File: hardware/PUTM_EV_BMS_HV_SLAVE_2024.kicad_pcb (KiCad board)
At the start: 2 copper layers, 187 parts, among them IC1 LTC6804HG-1#PBF, IC2 LTC6804HG-1#PBF, J1 L_LTC_CONN, J2 R_LTC_CONN, Q1 BCP56, Q10 CPH3351, Q11 CPH3351, Q12 BCP56, Q13 CPH3351, Q14 CPH3351, Q15 CPH3351, Q16 CPH3351, Q17 CPH3351, Q18 CPH3351, Q19 CPH3351, Q2 CPH3351, Q20 CPH3351, Q21 CPH3351, Q22 CPH3351, Q3 CPH3351, Q4 CPH3351, Q5 CPH3351, Q6 CPH3351, Q7 CPH3351, Q8 CPH3351, Q9 CPH3351

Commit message: spaced out version
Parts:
- removed C10, C11, C12, C13, C14, C15, C16, C17, C25, C26, C27, C28, C29, C30, C31, C32, C33, C34, C35, C36, C37, C38, C8, C9: 10nF, Capacitor_SMD:C_0603_1608Metric
- removed R1, R55, R56, R57, R58, R6: 10k, Resistor_SMD:R_0603_1608Metric
- removed R16, R24, R36, R40, R44, R48, R49, R50, R62, R66, R70, R74, R78, R82, R86, R90, R94, R98: 100, Resistor_SMD:R_0603_1608Metric
- added CN1: 100nF, Samacsys:CA064X104K4RACAUTO, F.Cu at (208.0, 95.5)
- added CN2: 100nF, Samacsys:CA064X104K4RACAUTO, F.Cu at (147.1, 52.5)
- added CN3: 100nF, Samacsys:CA064X104K4RACAUTO, F.Cu at (208.0, 91.2)
- added CN4: 100nF, Samacsys:CA064X104K4RACAUTO, F.Cu at (147.1, 56.8)
- added CN5: 100nF, Samacsys:CA064X104K4RACAUTO, F.Cu at (208.0, 86.8)
- added CN6: 100nF, Samacsys:CA064X104K4RACAUTO, F.Cu at (147.1, 61.1)
- added CN7: 100nF, Samacsys:CA064X104K4RACAUTO, F.Cu at (227.4, 88.7)
- added CN8: 100nF, Samacsys:CA064X104K4RACAUTO, F.Cu at (127.6, 59.3)
- added FL1: DLW21SN501SK2L, Samacsys:DLW21SN121HQ2L, F.Cu at (209.0, 80.9)
- added HS1: PAD, Connector_Wire:SolderWirePad_1x01_SMD_1x2mm, B.Cu at (196.7, 82.2)
- added HS10: PAD, Connector_Wire:SolderWirePad_1x01_SMD_1x2mm, B.Cu at (193.2, 95.8)
- added HS11: PAD, Connector_Wire:SolderWirePad_1x01_SMD_1x2mm, B.Cu at (161.8, 52.2)
- added HS12: PAD, Connector_Wire:SolderWirePad_1x01_SMD_1x2mm, B.Cu at (200.3, 65.8)
- added HS13: PAD, Connector_Wire:SolderWirePad_1x01_SMD_1x2mm, B.Cu at (214.3, 65.8)
- added HS14: PAD, Connector_Wire:SolderWirePad_1x01_SMD_1x2mm, B.Cu at (217.8, 52.2)
- added HS15: PAD, Connector_Wire:SolderWirePad_1x01_SMD_1x2mm, B.Cu at (158.3, 65.8)
- added HS16: PAD, Connector_Wire:SolderWirePad_1x01_SMD_1x2mm, B.Cu at (189.8, 52.2)
- added HS17: PAD, Connector_Wire:SolderWirePad_1x01_SMD_1x2mm, B.Cu at (203.8, 52.2)
- added HS18: PAD, Connector_Wire:SolderWirePad_1x01_SMD_1x2mm, B.Cu at (175.8, 52.2)
- added HS19: PAD, Connector_Wire:SolderWirePad_1x01_SMD_1x2mm, B.Cu at (186.3, 65.8)
- added HS2: PAD, Connector_Wire:SolderWirePad_1x01_SMD_1x2mm, B.Cu at (182.7, 82.2)
- added HS20: PAD, Connector_Wire:SolderWirePad_1x01_SMD_1x2mm, B.Cu at (172.3, 65.8)
- added HS3: PAD, Connector_Wire:SolderWirePad_1x01_SMD_1x2mm, B.Cu at (168.7, 82.2)
- added HS4: PAD, Connector_Wire:SolderWirePad_1x01_SMD_1x2mm, B.Cu at (154.7, 82.2)
- added HS5: PAD, Connector_Wire:SolderWirePad_1x01_SMD_1x2mm, B.Cu at (140.7, 82.2)
- added HS6: PAD, Connector_Wire:SolderWirePad_1x01_SMD_1x2mm, B.Cu at (137.2, 95.8)
- added HS7: PAD, Connector_Wire:SolderWirePad_1x01_SMD_1x2mm, B.Cu at (151.2, 95.8)
- added HS8: PAD, Connector_Wire:SolderWirePad_1x01_SMD_1x2mm, B.Cu at (165.2, 95.8)
- added HS9: PAD, Connector_Wire:SolderWirePad_1x01_SMD_1x2mm, B.Cu at (179.2, 95.8)
- added J3: M80-5100442, Samacsys:M80-51004YY, F.Cu at (225.2, 72.6)
- added J4: M80-5100442, Samacsys:M80-51004YY, F.Cu at (129.8, 74.3)
- added JP1: MES, Jumper:SolderJumper-2_P1.3mm_Bridged2Bar_RoundedPad1.0x1.5mm, F.Cu at (205.3, 59.0)
- added RN1: 100, Samacsys:EXBV8V101JV, F.Cu at (204.2, 95.5)
- added RN2: 100, Samacsys:EXBV8V101JV, F.Cu at (150.8, 52.5)
- added RN3: 100, Samacsys:EXBV8V101JV, F.Cu at (204.2, 91.2)
- added RN4: 100, Samacsys:EXBV8V101JV, F.Cu at (150.8, 56.8)
- added RN5: 100, Samacsys:EXBV8V101JV, F.Cu at (204.2, 86.8)
- added RN6: 100, Samacsys:EXBV8V101JV, F.Cu at (150.8, 61.1)
- added RN7: 10k, Samacsys:EXBV8V101JV, F.Cu at (227.4, 85.0)
- added RN8: 10k, Samacsys:EXBV8V101JV, F.Cu at (127.6, 63.1)
- added T1: HM1236NL, Samacsys:HM1236NL, F.Cu at (216.4, 73.6)
- added T3: HM1236NL, Samacsys:HM1236NL, F.Cu at (138.6, 73.3)
- C18, C23, C24, C3, Q1, Q10, Q11, Q12, Q13, Q14, Q15, Q16, Q17, Q18, Q19, Q2, Q20, Q21, Q22, Q3, Q4, Q5, Q6, Q7, Q8, Q9, R13, R17, R21, R25, R29, R33, R37, R41, R45, R5, R53, R59, R63, R67, R71, R75, R79, R83, R87, R9, R91, R95: moved to B.Cu
- C4, C5: value 10nF -> 100nF
- R12, R20, R28, R32: value 100 -> 120
- moved R12 293.6 mm to (220.9, 88.7), turned to -90 degrees
- moved C4 253.4 mm to (224.5, 88.7), turned to -90 degrees
- moved C2 251.5 mm to (222.1, 93.5), turned to -90 degrees
- moved C1 250.2 mm to (220.6, 93.5), turned to -90 degrees
- moved R2 249.3 mm to (224.5, 85.0), turned to 90 degrees
- moved C6 249.1 mm to (220.2, 81.5), turned to 180 degrees
- moved C3 247.1 mm to (218.2, 85.8)
- moved C18 240.9 mm to (215.8, 84.2)
- moved R5 239.0 mm to (214.2, 85.8)
- moved R7 237.1 mm to (216.2, 83.5), turned to 180 degrees
- moved R8 234.1 mm to (213.2, 83.5), turned to 180 degrees
- moved R4 232.3 mm to (207.5, 83.5), turned to 180 degrees
- moved C19 229.4 mm to (204.5, 83.5), turned to 180 degrees
- moved Q1 222.3 mm to (215.1, 91.2), turned to -90 degrees
- moved IC1 215.0 mm to (215.1, 91.2)
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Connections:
- net /L_LTC/DCH1/S renamed /L_LTC/S1
- net /L_LTC/DCH10/CO+ renamed /L_LTC/C11
- net /L_LTC/DCH10/S renamed /L_LTC/S11
- net /L_LTC/DCH2/S renamed /L_LTC/S2
- net /L_LTC/DCH3/S renamed /L_LTC/S3
- net /L_LTC/DCH4/S renamed /L_LTC/S4
- net /L_LTC/DCH5/S renamed /L_LTC/S5
- net /L_LTC/DCH6/S renamed /L_LTC/S7
- net /L_LTC/DCH7/S renamed /L_LTC/S8
- net /L_LTC/DCH8/S renamed /L_LTC/S9
- net /L_LTC/DCH9/S renamed /L_LTC/S10
- net /R_LTC/DCH1/S renamed /R_LTC/S1
- net /R_LTC/DCH10/CO+ renamed /R_LTC/C11
- net /R_LTC/DCH10/S renamed /R_LTC/S11
- net /R_LTC/DCH2/S renamed /R_LTC/S2
- net /R_LTC/DCH3/S renamed /R_LTC/S3
- net /R_LTC/DCH4/S renamed /R_LTC/S4
- net /R_LTC/DCH5/CO+ renamed /R_LTC/C5
- net /R_LTC/DCH5/S renamed /R_LTC/S5
- net /R_LTC/DCH6/S renamed /R_LTC/S7
- net /R_LTC/DCH7/S renamed /R_LTC/S8
- net /R_LTC/DCH8/S renamed /R_LTC/S9
- net /R_LTC/DCH9/S renamed /R_LTC/S10
- C4 pad 1: /TH1+ -> /TH5+
- C5 pad 1: /TH2+ -> /TH10+
- C5 pad 2: /C1- -> /C11-
- C6 pad 1: /TH3+ -> Net-(C6-Pad1)
- C6 pad 2: /C1- -> /C11-
- C7 pad 1: /TH4+ -> /C1-
- C7 pad 2: /C1- -> Net-(C7-Pad2)
- D3 pad 1: /C2+ -> /C2_SW+
- D6 pad 1: /SW_C5+ -> /C5+
- IC1 pad 10: /L_LTC/DCH7/CO+ -> /L_LTC/C8
- IC1 pad 12: /L_LTC/DCH6/CO+ -> /L_LTC/C7
- IC1 pad 14: /L_LTC/DCH5/CO+ -> /L_LTC/C5
- IC1 pad 15: unconnected-(IC1-S6-Pad15) -> /L_LTC/S6
- IC1 pad 16: /L_LTC/DCH5/CO+ -> /L_LTC/C5
- IC1 pad 18: /L_LTC/DCH4/CO+ -> /L_LTC/C4
- IC1 pad 20: /L_LTC/DCH3/CO+ -> /L_LTC/C3
- IC1 pad 22: /L_LTC/DCH2/CO+ -> /L_LTC/C2
- IC1 pad 24: /L_LTC/DCH1/CO+ -> /L_LTC/C1
- IC1 pad 26: /L_LTC/DCH1/F- -> /L_LTC/C0
- IC1 pad 3: unconnected-(IC1-S12-Pad3) -> /L_LTC/S12
- IC1 pad 33: unconnected-(IC1-GPIO5-Pad33) -> /TH5+
- IC1 pad 6: /L_LTC/DCH10/F- -> /L_LTC/C10
- IC1 pad 8: /L_LTC/DCH8/CO+ -> /L_LTC/C9
- IC2 pad 10: /R_LTC/DCH7/CO+ -> /R_LTC/C8
- IC2 pad 12: /R_LTC/DCH6/CO+ -> /R_LTC/C7
- IC2 pad 15: unconnected-(IC2-S6-Pad15) -> /R_LTC/S6
- IC2 pad 18: /R_LTC/DCH4/CO+ -> /R_LTC/C4
- IC2 pad 20: /R_LTC/DCH3/CO+ -> /R_LTC/C3
- IC2 pad 22: /R_LTC/DCH2/CO+ -> /R_LTC/C2
- IC2 pad 24: /R_LTC/DCH1/CO+ -> /R_LTC/C1
- IC2 pad 26: /R_LTC/DCH1/F- -> /R_LTC/C0
- IC2 pad 27: /TH5+ -> /TH6+
- IC2 pad 28: /TH6+ -> /TH7+
- IC2 pad 29: /TH7+ -> /TH8+
- IC2 pad 3: unconnected-(IC2-S12-Pad3) -> /R_LTC/S12
- IC2 pad 32: /TH8+ -> /TH9+
- IC2 pad 33: unconnected-(IC2-GPIO5-Pad33) -> /TH10+
- IC2 pad 41: /L_LTC/IMB -> /R_LTC/IMA
- IC2 pad 42: /L_LTC/IPB -> /R_LTC/IPA
- IC2 pad 6: /R_LTC/DCH10/F- -> /R_LTC/C10
- IC2 pad 8: /R_LTC/DCH8/CO+ -> /R_LTC/C9
- J1 pad 10: /C1- -> /TH5+
- J1 pad 11: /TH3+ -> /C1-
- J1 pad 13: /TH2+ -> /TH3+
- J1 pad 14: /C1- -> /TH4+
- J1 pad 6: /C1- -> unconnected-(J1-Pin_6-Pad6)
- J1 pad 9: /TH4+ -> /TH2+
- J2 pad 10: /C11- -> /TH10+
- J2 pad 11: /TH7+ -> /C11-
- J2 pad 13: /TH6+ -> unconnected-(J2-Pin_13-Pad13)
- J2 pad 14: /C11- -> /TH9+
- J2 pad 15: unconnected-(J2-Pin_15-Pad15) -> /TH8+
- J2 pad 5: /TH5+ -> /TH6+
- J2 pad 6: /C11- -> unconnected-(J2-Pin_6-Pad6)
- J2 pad 9: /TH8+ -> /TH7+
- Q3 pad 2: /C2+ -> /C2_SW+
- Q6 pad 2: /SW_C5+ -> /C5+
- R12 pad 1: /L_LTC/DCH1/CO+ -> /IPA
- R12 pad 2: /C1+ -> /IMA
- R17 pad 2: /C2+ -> /C2_SW+
- R2 pad 1: /L_LTC/VREF2 -> /TH5+
- R2 pad 2: /TH2+ -> /L_LTC/VREF2
- R20 pad 1: /L_LTC/DCH3/CO+ -> /L_LTC/IPB
- R20 pad 2: /C3+ -> /L_LTC/IMB
- R28 pad 1: /L_LTC/DCH5/CO+ -> /R_LTC/IPA
- R28 pad 2: /SW_C5+ -> /R_LTC/IMA
- R29 pad 2: /SW_C5+ -> /C5+
- R3 pad 1: /L_LTC/VREF2 -> /TH10+
- R3 pad 2: /TH3+ -> /R_LTC/VREF2
- R32 pad 1: /L_LTC/DCH6/CO+ -> /IPB
- R32 pad 2: /C6+ -> /IMB
- S1 pad 1: /C5+ -> /C2+
- S1 pad 2: /SW_C5+ -> /C2_SW+
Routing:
- net /R_LTC/C0: track 0.00 -> 14.3 mm
- net /L_LTC/C0: track 0.00 -> 14.3 mm
- net /R_LTC/C5: track 0.00 -> 10.3 mm
- net /L_LTC/C5: track 0.00 -> 10.3 mm
- net /R_LTC/C11: track 0.00 -> 10.2 mm
- net /L_LTC/C11: track 0.00 -> 10.2 mm
- net Net-(Q1-C): track 0.00 -> 10.1 mm
- net Net-(Q12-C): track 0.00 -> 10.1 mm
- net /L_LTC/VREG: track 0.00 -> 8.94 mm, vias 0 -> 1
- net /R_LTC/VREG: track 0.00 -> 8.68 mm, vias 0 -> 1
- net /L_LTC/C9: track 0.00 -> 8.29 mm
- net /R_LTC/C9: track 0.00 -> 8.29 mm
- net /R_LTC/C4: track 0.00 -> 8.02 mm
- net /L_LTC/C4: track 0.00 -> 8.02 mm
- net /L_LTC/VREF2: track 0.00 -> 8.01 mm
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- added copper zone on B.Cu, net Net-(Q10-D)
- added copper zone on B.Cu, net Net-(Q11-D)
- added copper zone on B.Cu, net Net-(Q13-D)
- added copper zone on B.Cu, net Net-(Q14-D)
- added copper zone on B.Cu, net Net-(Q15-D)
- added copper zone on B.Cu, net Net-(Q16-D)
- added copper zone on B.Cu, net Net-(Q17-D)
- added copper zone on B.Cu, net Net-(Q18-D)
- added copper zone on B.Cu, net Net-(Q19-D)
- added copper zone on B.Cu, net Net-(Q2-D)
- added copper zone on B.Cu, net Net-(Q20-D)
- added copper zone on B.Cu, net Net-(Q21-D)
- added copper zone on B.Cu, net Net-(Q22-D)
- added copper zone on B.Cu, net Net-(Q3-D)
- added copper zone on B.Cu, net Net-(Q4-D)
- added copper zone on B.Cu, net Net-(Q5-D)
- added copper zone on B.Cu, net Net-(Q6-D)
- added copper zone on B.Cu, net Net-(Q7-D)
- added copper zone on B.Cu, net Net-(Q8-D)
- added copper zone on B.Cu, net Net-(Q9-D)
- added copper zone on B.Cu, net THERMAL
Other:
- board outline added: 105 x 48 mm
- copper layers 2 -> 4

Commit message: finished layout
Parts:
- removed HS1, HS10, HS11, HS12, HS13, HS14, HS15, HS16, HS17, HS18, HS19, HS2, HS20, HS3, HS4, HS5, HS6, HS7, HS8, HS9: PAD, Connector_Wire:SolderWirePad_1x01_SMD_1x2mm
- added F1: 6V/6A, Samacsys:1206L075SLYR, B.Cu at (193.8, 82.2)
- added F10: 6V/6A, Samacsys:1206L075SLYR, B.Cu at (198.1, 95.8)
- added F11: 6V/6A, Samacsys:1206L075SLYR, B.Cu at (156.9, 52.2)
- added F12: 6V/6A, Samacsys:1206L075SLYR, B.Cu at (203.2, 65.8)
- added F13: 6V/6A, Samacsys:1206L075SLYR, B.Cu at (217.2, 65.8)
- added F14: 6V/6A, Samacsys:1206L075SLYR, B.Cu at (212.9, 52.2)
- added F15: 6V/6A, Samacsys:1206L075SLYR, B.Cu at (161.2, 65.8)
- added F16: 6V/6A, Samacsys:1206L075SLYR, B.Cu at (184.9, 52.2)
- added F17: 6V/6A, Samacsys:1206L075SLYR, B.Cu at (198.9, 52.2)
- added F18: 6V/6A, Samacsys:1206L075SLYR, B.Cu at (170.9, 52.2)
- added F19: 6V/6A, Samacsys:1206L075SLYR, B.Cu at (189.2, 65.8)
- added F2: 6V/6A, Samacsys:1206L075SLYR, B.Cu at (179.8, 82.2)
- added F20: 6V/6A, Samacsys:1206L075SLYR, B.Cu at (175.2, 65.8)
- added F3: 6V/6A, Samacsys:1206L075SLYR, B.Cu at (165.8, 82.2)
- added F4: 6V/6A, Samacsys:1206L075SLYR, B.Cu at (151.8, 82.2)
- added F5: 6V/6A, Samacsys:1206L075SLYR, B.Cu at (137.8, 82.2)
- added F6: 6V/6A, Samacsys:1206L075SLYR, B.Cu at (142.1, 95.8)
- added F7: 6V/6A, Samacsys:1206L075SLYR, B.Cu at (156.1, 95.8)
- added F8: 6V/6A, Samacsys:1206L075SLYR, B.Cu at (170.1, 95.8)
- added F9: 6V/6A, Samacsys:1206L075SLYR, B.Cu at (184.1, 95.8)
- added J5: Conn_01x01_Pin, Connector_Wire:SolderWire-0.1sqmm_1x01_D0.4mm_OD1mm_Relief, F.Cu at (133.8, 76.6)
- added J6: Conn_01x01_Pin, Connector_Wire:SolderWire-0.1sqmm_1x01_D0.4mm_OD1mm_Relief, F.Cu at (221.2, 71.4)
- added REF**: plate, Samacsys:plate, B.Cu at (177.5, 74.0)
- R13, R17, R21, R25, R29, R33, R37, R41, R45, R59, R63, R67, R71, R75, R79, R83, R87, R9, R91, R95: footprint Resistor_SMD:R_2512_6332Metric -> Samacsys:RESC6331X80N
- moved J3 95.5 mm to (129.7, 75.0), turned to 90 degrees
- moved J4 95.5 mm to (225.3, 73.0), turned to -90 degrees
- moved T3 78.0 mm to (216.5, 77.7), turned to 0 degrees
- moved T1 77.9 mm to (138.6, 70.3), turned to 180 degrees
- moved C6 75.3 mm to (145.4, 72.7), turned to 90 degrees
- moved FL1 63.2 mm to (146.9, 68.7), turned to -90 degrees
- moved C7 62.7 mm to (209.6, 75.3), turned to 90 degrees
- moved C5 5.43 mm to (126.8, 63.2), turned to -90 degrees
- moved C4 5.36 mm to (228.2, 84.9), turned to 90 degrees
- moved R3 5.25 mm to (126.8, 59.4), turned to 90 degrees
- moved R2 5.18 mm to (228.2, 88.6), turned to -90 degrees
- moved CN8 4.43 mm to (129.7, 63.2), turned to 0 degrees
- moved CN7 4.34 mm to (225.3, 84.9), turned to 180 degrees
- moved RN8 4.21 mm to (129.7, 59.4), turned to 0 degrees
- moved RN7 4.12 mm to (225.3, 88.6), turned to 180 degrees
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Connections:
- C4 pad 1: /TH5+ -> /TH1+
- C5 pad 1: /TH10+ -> /TH6+
- CN7 pad 5: /TH1+ -> /TH5+
- CN7 pad 6: /TH2+ -> /TH4+
- CN7 pad 8: /TH4+ -> /TH2+
- CN8 pad 5: /TH6+ -> /TH10+
- CN8 pad 6: /TH7+ -> /TH9+
- CN8 pad 8: /TH9+ -> /TH7+
- D17 pad 1: /C11+ -> /C11_SW+
- D3 pad 1: /C2_SW+ -> /C2+
- J3 pad 4: Net-(J3-Pin_2) -> Net-(J3-Pin_3)
- J4 pad 2: Net-(J3-Pin_2) -> Net-(J4-Pin_2)
- J4 pad 4: Net-(J3-Pin_2) -> Net-(J4-Pin_3)
- JP1 pad 1: /C2+ -> /C11+
- JP1 pad 2: /C2_SW+ -> /C11_SW+
- Q16 pad 2: /C11+ -> /C11_SW+
- Q3 pad 2: /C2_SW+ -> /C2+
- R10 pad 1: Net-(Q2-D) -> Net-(F1-Pad1)
- R13 pad 1: Net-(Q3-D) -> Net-(F2-Pad1)
- R14 pad 1: Net-(Q3-D) -> Net-(F2-Pad1)
- R17 pad 1: Net-(Q4-D) -> Net-(F3-Pad1)
- R17 pad 2: /C2_SW+ -> /C2+
- R18 pad 1: Net-(Q4-D) -> Net-(F3-Pad1)
- R2 pad 1: /TH5+ -> /TH1+
- R21 pad 1: Net-(Q5-D) -> Net-(F4-Pad1)
- R22 pad 1: Net-(Q5-D) -> Net-(F4-Pad1)
- R25 pad 1: Net-(Q6-D) -> Net-(F5-Pad1)
- R26 pad 1: Net-(Q6-D) -> Net-(F5-Pad1)
- R29 pad 1: Net-(Q7-D) -> Net-(F6-Pad1)
- R3 pad 1: /TH10+ -> /TH6+
- R30 pad 1: Net-(Q7-D) -> Net-(F6-Pad1)
- R33 pad 1: Net-(Q8-D) -> Net-(F7-Pad1)
- R34 pad 1: Net-(Q8-D) -> Net-(F7-Pad1)
- R37 pad 1: Net-(Q9-D) -> Net-(F8-Pad1)
- R38 pad 1: Net-(Q9-D) -> Net-(F8-Pad1)
- R41 pad 1: Net-(Q10-D) -> Net-(F9-Pad1)
- R42 pad 1: Net-(Q10-D) -> Net-(F9-Pad1)
- R45 pad 1: Net-(Q11-D) -> Net-(F10-Pad1)
- R46 pad 1: Net-(Q11-D) -> Net-(F10-Pad1)
- R59 pad 1: Net-(Q13-D) -> Net-(F11-Pad1)
- R60 pad 1: Net-(Q13-D) -> Net-(F11-Pad1)
- R63 pad 1: Net-(Q14-D) -> Net-(F12-Pad1)
- R64 pad 1: Net-(Q14-D) -> Net-(F12-Pad1)
- R67 pad 1: Net-(Q15-D) -> Net-(F13-Pad1)
- R68 pad 1: Net-(Q15-D) -> Net-(F13-Pad1)
- R71 pad 1: Net-(Q16-D) -> Net-(F14-Pad1)
- R72 pad 1: Net-(Q16-D) -> Net-(F14-Pad1)
- R75 pad 1: Net-(Q17-D) -> Net-(F15-Pad1)
- R76 pad 1: Net-(Q17-D) -> Net-(F15-Pad1)
- R79 pad 1: Net-(Q18-D) -> Net-(F16-Pad1)
- R80 pad 1: Net-(Q18-D) -> Net-(F16-Pad1)
- R83 pad 1: Net-(Q19-D) -> Net-(F17-Pad1)
- R83 pad 2: /C11+ -> /C11_SW+
- R84 pad 1: Net-(Q19-D) -> Net-(F17-Pad1)
- R87 pad 1: Net-(Q20-D) -> Net-(F18-Pad1)
- R88 pad 1: Net-(Q20-D) -> Net-(F18-Pad1)
- R9 pad 1: Net-(Q2-D) -> Net-(F1-Pad1)
- R91 pad 1: Net-(Q21-D) -> Net-(F19-Pad1)
- R92 pad 1: Net-(Q21-D) -> Net-(F19-Pad1)
- R95 pad 1: Net-(Q22-D) -> Net-(F20-Pad1)
- R96 pad 1: Net-(Q22-D) -> Net-(F20-Pad1)
- RN1 pad 2: /C2_SW+ -> /C2+
- RN2 pad 3: /C11+ -> /C11_SW+
- RN7 pad 1: /TH4+ -> /TH2+
- RN7 pad 3: /TH2+ -> /TH4+
- RN7 pad 4: /TH1+ -> /TH5+
- RN8 pad 1: /TH9+ -> /TH7+
- RN8 pad 3: /TH7+ -> /TH9+
- RN8 pad 4: /TH6+ -> /TH10+
- S1 pad 1: /C2+ -> /C11+
- S1 pad 2: /C2_SW+ -> /C11_SW+
- T1 pad 4: Net-(J3-Pin_1) -> Net-(J3-Pin_2)
- T1 pad 5: Net-(J3-Pin_3) -> Net-(J3-Pin_1)
- T3 pad 4: Net-(J4-Pin_1) -> Net-(J4-Pin_2)
- T3 pad 5: Net-(J4-Pin_3) -> Net-(J4-Pin_1)
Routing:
- net /C11-: track 1.47 -> 139.0 mm, vias 1 -> 9
- net /C1-: track 5.04 -> 112.6 mm, vias 1 -> 7
- net /R_LTC/S1: track 0.00 -> 95.4 mm, vias 0 -> 2
- net /L_LTC/S5: track 0.00 -> 90.9 mm, vias 0 -> 2
- net /L_LTC/IPB: track 2.50 -> 92.9 mm, vias 0 -> 2
- net /L_LTC/IMB: track 2.50 -> 91.9 mm, vias 0 -> 2
- net /L_LTC/S7: track 0.00 -> 86.5 mm, vias 0 -> 2
- net /L_LTC/S4: track 0.00 -> 83.4 mm, vias 0 -> 2
- net /R_LTC/S11: track 0.00 -> 81.0 mm, vias 0 -> 2
- net /TH6+: track 4.98 -> 83.2 mm
- net /R_LTC/S2: track 0.00 -> 74.6 mm, vias 0 -> 2
- net /L_LTC/S8: track 0.00 -> 74.5 mm, vias 0 -> 2
- net /TH8+: track 5.00 -> 78.7 mm
- net /TH7+: track 5.34 -> 78.4 mm
- net /L_LTC/S3: track 0.00 -> 71.3 mm, vias 0 -> 2
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- added copper zone on B.Cu, net /C1+
- added copper zone on B.Cu, net /C1-
- added copper zone on B.Cu, net /C10+
- added copper zone on B.Cu, net /C11+
- added copper zone on F.Cu, net /C11+
- added copper zone on B.Cu, net /C11-
- added copper zone on B.Cu, net /C11_SW+
- added copper zone on F.Cu, net /C11_SW+
- added copper zone on B.Cu, net /C12+
- added copper zone on F.Cu, net /C12+
- added copper zone on B.Cu, net /C13+
- added copper zone on B.Cu, net /C14+
- added copper zone on B.Cu, net /C15+
- added copper zone on B.Cu, net /C16+
- added copper zone on B.Cu, net /C17+
- added copper zone on B.Cu, net /C18+
- added copper zone on F.Cu, net /C18+
- added copper zone on B.Cu, net /C19+
- added copper zone on B.Cu, net /C2+
- added copper zone on B.Cu, net /C20+
- added copper zone on B.Cu, net /C3+
- added copper zone on B.Cu, net /C4+
- added copper zone on B.Cu, net /C5+
- added copper zone on B.Cu, net /C6+
- added copper zone on F.Cu, net /C6+
- added copper zone on B.Cu, net /C7+
- added copper zone on B.Cu, net /C8+
- added copper zone on B.Cu, net /C9+
- added copper zone on B.Cu, net Net-(F1-Pad1)
- added copper zone on B.Cu, net Net-(F10-Pad1)
- added copper zone on B.Cu, net Net-(F11-Pad1)
- added copper zone on B.Cu, net Net-(F12-Pad1)
- added copper zone on B.Cu, net Net-(F13-Pad1)
- added copper zone on B.Cu, net Net-(F14-Pad1)
- added copper zone on B.Cu, net Net-(F15-Pad1)
- added copper zone on B.Cu, net Net-(F16-Pad1)
- added copper zone on B.Cu, net Net-(F17-Pad1)
- added copper zone on B.Cu, net Net-(F18-Pad1)
- added copper zone on B.Cu, net Net-(F19-Pad1)
- added copper zone on B.Cu, net Net-(F2-Pad1)
- added copper zone on B.Cu, net Net-(F20-Pad1)
- added copper zone on B.Cu, net Net-(F3-Pad1)
- added copper zone on B.Cu, net Net-(F4-Pad1)
- added copper zone on B.Cu, net Net-(F5-Pad1)
- added copper zone on B.Cu, net Net-(F6-Pad1)
- added copper zone on B.Cu, net Net-(F7-Pad1)
- added copper zone on B.Cu, net Net-(F8-Pad1)
- added copper zone on B.Cu, net Net-(F9-Pad1)
- removed copper zone on B.Cu, net THERMAL
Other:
- board text added: "-> front of battery"
- board text added: "IN"
- board text added: "OUT"

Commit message: final version
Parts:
- removed REF**: plate, Samacsys:plate
- moved H1 2.50 mm to (226.5, 56.0)
- moved H2 2.50 mm to (128.5, 56.0)
- moved H3 2.50 mm to (128.5, 92.0)
- moved H4 2.50 mm to (226.5, 92.0)
- moved C5 2.39 mm to (125.8, 65.4)
- moved CN8 2.39 mm to (128.7, 65.4)
- moved R3 2.39 mm to (125.8, 61.6)
- moved RN8 2.39 mm to (128.7, 61.6)
- moved C4 2.39 mm to (229.2, 82.7)
- moved CN7 2.39 mm to (226.3, 82.7)
- moved R2 2.39 mm to (229.2, 86.4)
- moved RN7 2.39 mm to (226.3, 86.4)
- moved J3 1.80 mm to (129.7, 76.8)
- moved J4 1.75 mm to (225.3, 71.2)
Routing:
- net /TH3+: track 71.9 -> 86.1 mm
- net /TH2+: track 69.9 -> 82.8 mm
- net /TH1+: track 74.1 -> 86.1 mm
- net Net-(J3-Pin_3): track 9.12 -> 18.7 mm
- net Net-(J4-Pin_3): track 9.09 -> 18.7 mm
- net /TH8+: track 78.7 -> 85.8 mm
- net /TH4+: track 69.1 -> 76.0 mm
- net /TH10+: track 63.2 -> 69.9 mm
- net /TH9+: track 60.3 -> 66.7 mm
- net /TH5+: track 62.8 -> 68.1 mm
- net /TH7+: track 78.4 -> 83.1 mm
- net /TH6+: track 83.2 -> 87.7 mm
- net Net-(J4-Pin_2): track 7.51 -> 9.94 mm
- net /C1-: track 112.6 -> 114.5 mm
- net Net-(J3-Pin_2): track 8.15 -> 10.0 mm
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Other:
- outline, holes or cut-outs redrawn

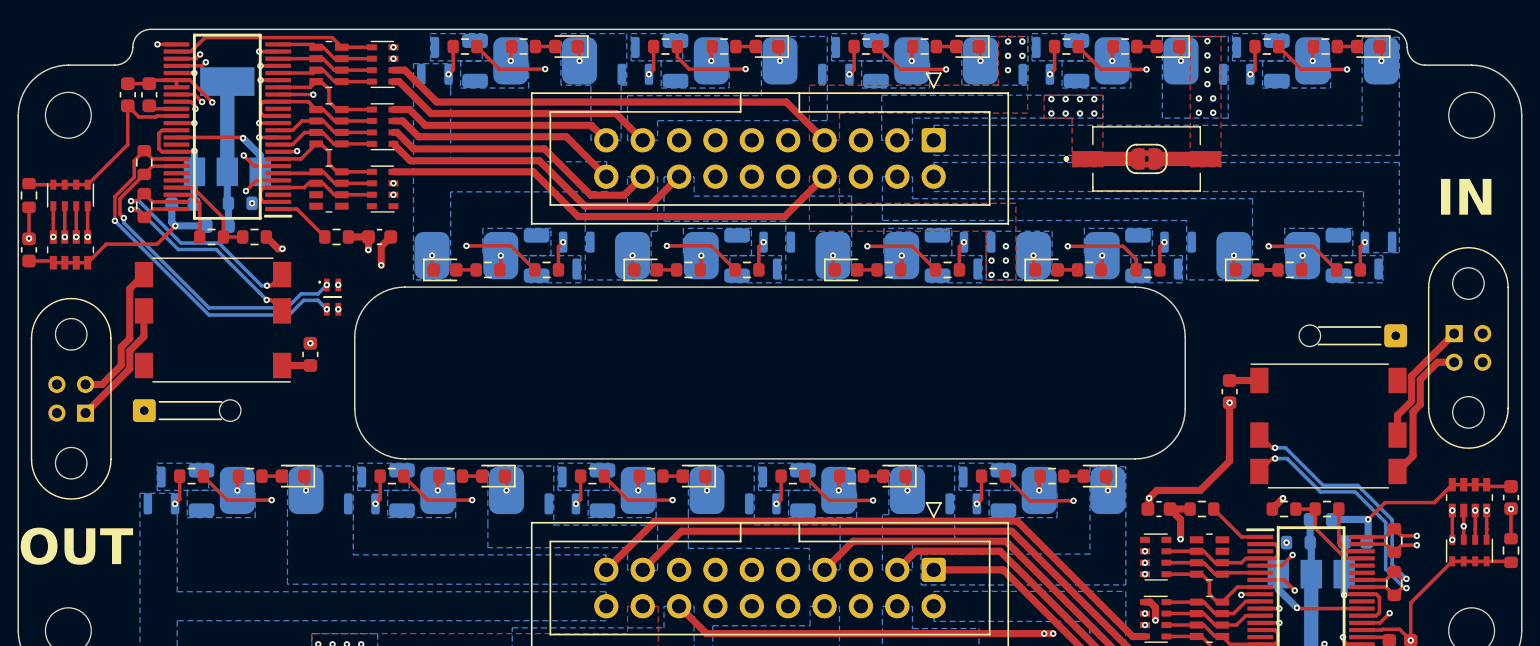
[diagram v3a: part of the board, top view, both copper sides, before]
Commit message: change from transformator to capacitive isolation between ltc, change ibias/icmp pin since they are incorrectly connected
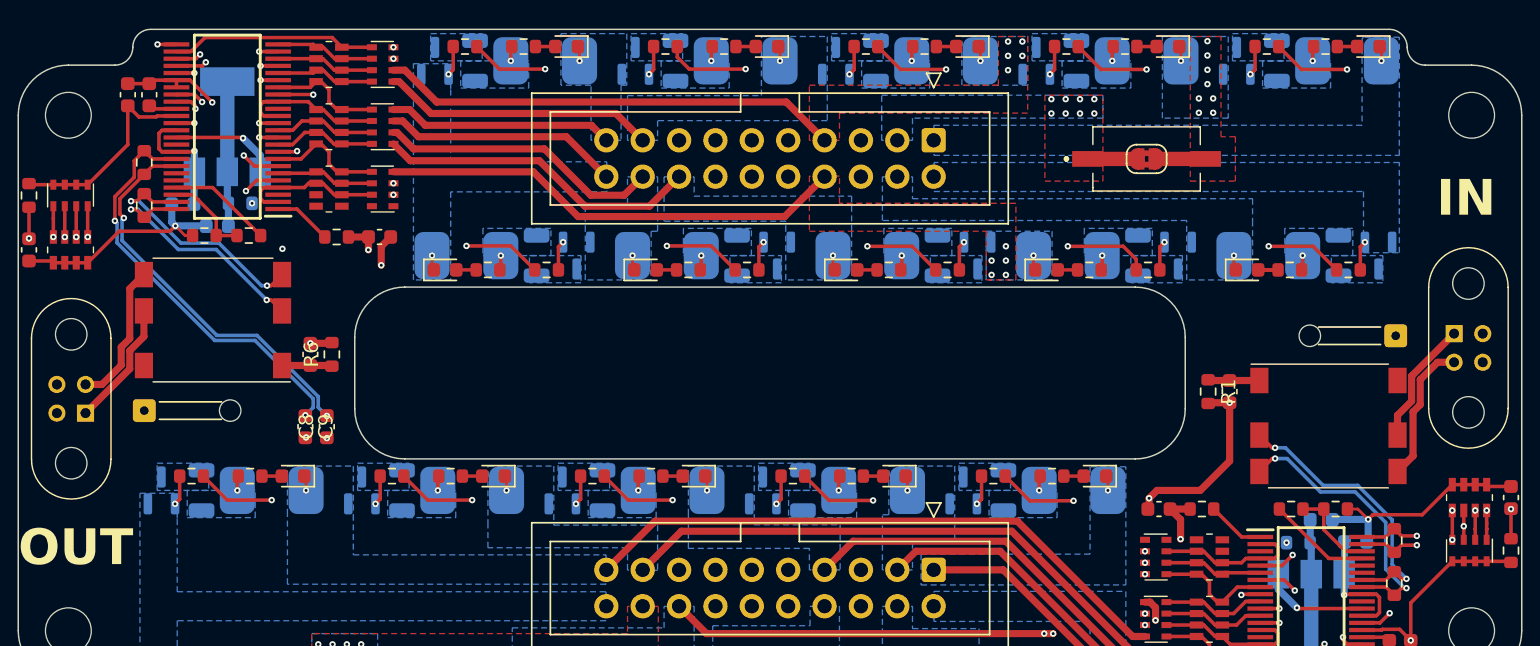
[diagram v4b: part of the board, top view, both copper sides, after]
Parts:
- removed FL1: DLW21SN501SK2L, Samacsys:DLW21SN121HQ2L
- added C8: 10nF/50V, Capacitor_SMD:C_0603_1608Metric, F.Cu at (146.6, 77.8)
- added C9: 10nF/50V, Capacitor_SMD:C_0603_1608Metric, F.Cu at (145.1, 77.8)
- added R1: 10k, Resistor_SMD:R_0603_1608Metric, F.Cu at (208.1, 75.3)
- added R6: 10k, Resistor_SMD:R_0603_1608Metric, F.Cu at (146.9, 72.7)
- C18, C19, C20, C24: value 100nf -> 100nF
- CN1, CN2, CN3, CN4, CN5, CN6, CN7, CN8: value 100nF -> 4x100nF
- F1, F10, F11, F12, F13, F14, F15, F16, F17, F18, F19, F2, F20, F3, F4, F5, F6, F7, F8, F9: value 6V/6A -> 1206L600SLWR
- J1: value L_LTC_CONN -> TST-110-01-T-D
- J2: value R_LTC_CONN -> TST-110-01-T-D
- RN1, RN2, RN3, RN4, RN5, RN6: value 100 -> 4x100
- RN7, RN8: value 10k -> 4x10k
- moved R8 3.60 mm to (217.0, 83.5), turned to 0 degrees
- moved R54 3.50 mm to (138.0, 64.4), turned to 180 degrees
- moved R52 2.60 mm to (141.1, 64.4), turned to 180 degrees
- moved R7 2.50 mm to (213.9, 83.5), turned to 0 degrees
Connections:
- net Net-(J3-Pin_1) renamed /OUT+
- net Net-(J3-Pin_2) renamed /OUT-
- net Net-(J4-Pin_1) renamed /IN+
- net Net-(J4-Pin_2) renamed /IN-
- R52 pad 1: Net-(IC2-ICMP) -> Net-(IC2-IBIAS)
- R52 pad 2: Net-(IC2-IBIAS) -> Net-(IC2-ICMP)
- R54 pad 1: Net-(IC2-IBIAS) -> Net-(IC2-ICMP)
- R7 pad 1: Net-(IC1-ICMP) -> Net-(IC1-IBIAS)
- R7 pad 2: Net-(IC1-IBIAS) -> Net-(IC1-ICMP)
- R8 pad 1: Net-(IC1-IBIAS) -> Net-(IC1-ICMP)
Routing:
- net /L_LTC/IPB: track 92.8 -> 84.7 mm
- net /L_LTC/IMB: track 91.7 -> 85.7 mm
- net /R_LTC/IPA: track 24.0 -> 27.8 mm
- net /R_LTC/IMA: track 26.4 -> 29.4 mm
- net /C1-: track 114.5 -> 116.7 mm, vias 7 -> 6
- net Net-(IC1-ICMP): track 4.21 -> 6.18 mm
- net Net-(IC2-ICMP): track 4.21 -> 6.12 mm
- net /C11-: track 138.1 -> 139.6 mm
- net Net-(C7-Pad2): track 2.08 -> 3.60 mm
- net Net-(C6-Pad1): track 1.97 -> 3.50 mm

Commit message: new 1.2 revision
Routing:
- net /IN-: track 9.94 -> 9.26 mm
- net /OUT-: track 10.0 -> 9.36 mm
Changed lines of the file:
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@@
 	)
 	(segment
-		(start 133.775 71.455024)
+		(start 129.7 76.8)
+		(end 131.65 74.85)
+		(width 0.25)
+		(layer "F.Cu")
+		(net 163)
+	)
+	(segment
+		(start 131.65 74.85)
+		(end 131.65 71.79)
+		(width 0.25)
+		(layer "F.Cu")
+		(net 163)
+	)
+	(segment
+		(start 131.65 71.79)
 		(end 133.775 69.665)
-		(width 0.5)
-		(layer "F.Cu")
-		(net 163)
-	)
-	(segment
-		(start 129.7 76.8)
-		(end 132.79 73.71)
-		(width 0.5)
-		(layer "F.Cu")
-		(net 163)
-	)
-	(segment
-		(start 132.79 72.440024)
-		(end 133.775 71.455024)
-		(width 0.5)
-		(layer "F.Cu")
-		(net 163)
-	)
-	(segment
-		(start 132.79 73.71)
-		(end 132.79 72.440024)
-		(width 0.5)
+		(width 0.25)
 		(layer "F.Cu")
 		(net 163)
@@
 	)
 	(segment
-		(start 130.851472 74.8)
-		(end 132.19 73.461472)
-		(width 0.5)
+		(start 129.7 74.8)
+		(end 131.3 73.2)
+		(width 0.25)
 		(layer "F.Cu")
 		(net 180)
 	)
 	(segment
-		(start 129.7 74.8)
-		(end 130.851472 74.8)
-		(width 0.5)
+		(start 131.3 69.6)
+		(end 133.775 67.125)
+		(width 0.25)
 		(layer "F.Cu")
 		(net 180)
 	)
 	(segment
-		(start 132.19 73.461472)
-		(end 132.19 72.191496)
-		(width 0.5)
-		(layer "F.Cu")
-		(net 180)
-	)
-	(segment
-		(start 132.79 68.11)
-		(end 133.775 67.125)
-		(width 0.5)
-		(layer "F.Cu")
-		(net 180)
-	)
-	(segment
-		(start 132.79 71.591496)
-		(end 132.79 68.11)
-		(width 0.5)
-		(layer "F.Cu")
-		(net 180)
-	)
-	(segment
-		(start 132.19 72.191496)
-		(end 132.79 71.591496)
-		(width 0.5)
+		(start 131.3 73.2)
+		(end 131.3 69.6)
+		(width 0.25)
 		(layer "F.Cu")
 		(net 180)
@@
 	)
 	(segment
-		(start 222.31 74.215)
-		(end 225.275 71.25)
-		(width 0.5)
+		(start 223.3 76.36)
+		(end 221.325 78.335)
+		(width 0.25)
 		(layer "F.Cu")
 		(net 182)
 	)
 	(segment
-		(start 222.31 75.965)
-		(end 222.31 74.215)
-		(width 0.5)
+		(start 223.3 73.225)
+		(end 223.3 76.36)
+		(width 0.25)
 		(layer "F.Cu")
 		(net 182)
 	)
 	(segment
-		(start 221.325 78.335)
-		(end 221.325 76.95)
-		(width 0.5)
+		(start 225.275 71.25)
+		(end 223.3 73.225)
+		(width 0.25)
 		(layer "F.Cu")
 		(net 182)
 	)
 	(segment
-		(start 221.325 76.95)
-		(end 222.31 75.965)
-		(width 0.5)
-		(layer "F.Cu")
-		(net 182)
-	)
-	(segment
-		(start 222.91 76.213528)
-		(end 222.91 74.463528)
-		(width 0.5)
+		(start 223.65 78.55)
+		(end 221.325 80.875)
+		(width 0.25)
 		(layer "F.Cu")
 		(net 183)
 	)
 	(segment
-		(start 221.325 80.875)
-		(end 222.41 79.79)
-		(width 0.5)
+		(start 223.65 74.875)
+		(end 223.65 78.55)
+		(width 0.25)
 		(layer "F.Cu")
 		(net 183)
 	)
 	(segment
-		(start 222.91 74.463528)
-		(end 224.123528 73.25)
-		(width 0.5)
+		(start 225.275 73.25)
+		(end 223.65 74.875)
+		(width 0.25)
 		(layer "F.Cu")
 		(net 183)
-	)
-	(segment
-		(start 222.41 76.713528)
-		(end 222.91 76.213528)
-		(width 0.5)
-		(layer "F.Cu")
-		(net 183)
-	)
-	(segment
-		(start 224.123528 73.25)
-		(end 225.275 73.25)
-		(width 0.5)
-		(layer "F.Cu")
-		(net 183)
-	)
-	(segment
-		(start 222.41 79.79)
-		(end 222.41 76.713528)
-		(width 0.5)
-		(layer "F.Cu")
-		(net 183)
